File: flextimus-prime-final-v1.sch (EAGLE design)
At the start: 40 parts, among them T1 2N2222, U1 STM32F042K6, U2 IP4220CZ6, U3 MCP1802T-3302I/OT

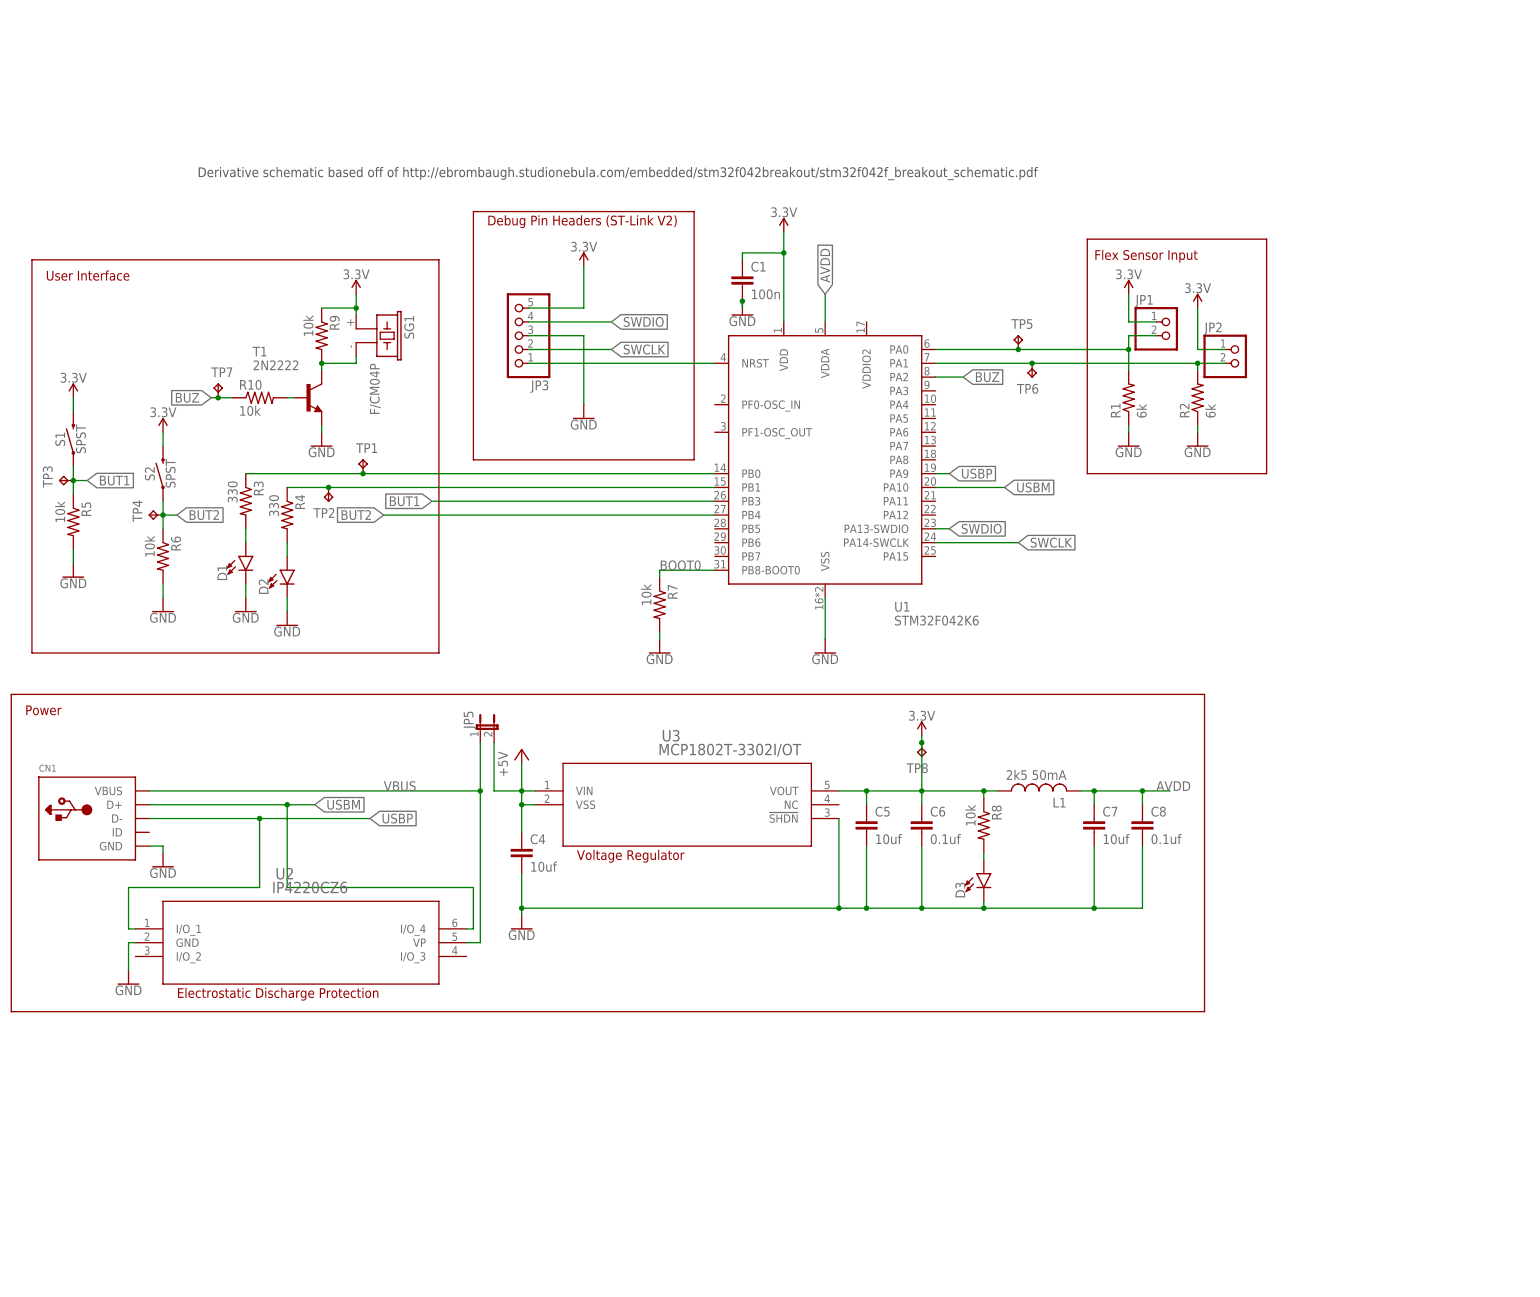
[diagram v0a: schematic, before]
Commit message: Add new board layout and schematic
Also add new lcd driver to use later
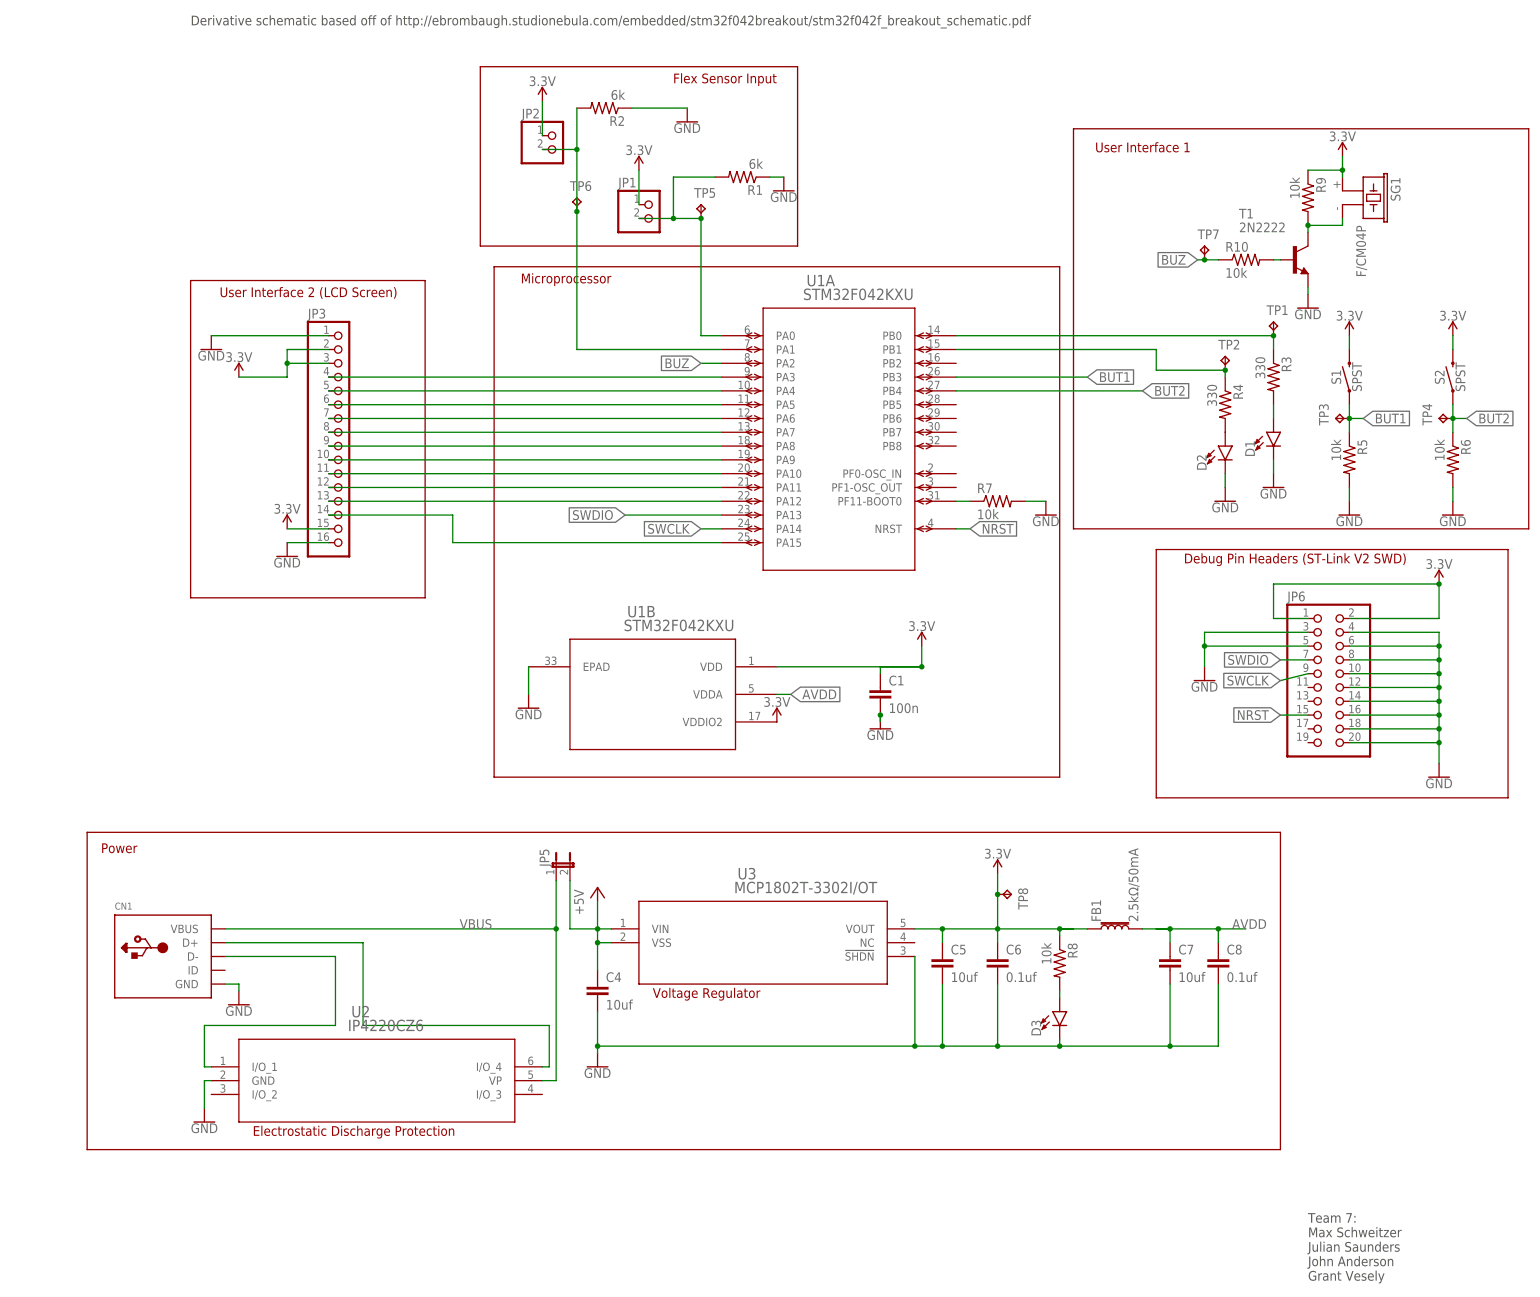
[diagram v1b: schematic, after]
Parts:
- removed L1: 2k5 50mA, rcl:L-USL3216C
- added FB1: 2.5kΩ/50mA, SparkFun-Coils:FERRITE_BEAD-0603
- added JP6: (no value), pinhead:PINHD-2X10
- JP3: device pinhead:PINHD-1X5 -> pinhead:PINHD-1X16
- U1: value STM32F042K6 -> STM32F042KXU; device STM32F042K:STM32F042K6 -> 411test:STM32F042KXU
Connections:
- removed net BOOT0: R7.1, U1.PB8-BOOT0
- new net N$10: JP3.4, U1A.PA3
- new net N$11: JP3.5, U1A.PA4
- new net N$12: JP3.6, U1A.PA5
- new net N$13: JP3.7, U1A.PA6
- new net N$14: JP3.8, U1A.PA7
- new net N$15: JP3.9, U1A.PA8
- new net N$16: JP3.10, U1A.PA9
- new net N$17: JP3.11, U1A.PA10
- new net N$18: JP3.12, U1A.PA11
- new net N$19: JP3.13, U1A.PA12
- new net N$20: R7.1, U1A.PF11-BOOT0
- new net N$21: R4.1, TP2.TP, U1A.PB1
- net 3.3V: now also FB1.1, JP3.15, JP3.2, JP3.3, JP6.1, JP6.2, U1B.VDD, U1B.VDDIO2; no longer JP3.5, L1.1, U1.VDD
- net AVDD: now also FB1.2, U1B.VDDA; no longer L1.2, U1.VDDA
- net BUT1: now also U1A.PB3; no longer U1.PB3
- net BUT2: now also U1A.PB4; no longer U1.PB4
- net BUZ: now also U1A.PA2; no longer U1.PA2
- net GND: now also JP3.1, JP3.16, JP6.10, JP6.12, JP6.14, JP6.16, JP6.18, JP6.20, JP6.3, JP6.4, JP6.5, JP6.6, JP6.8, U1B.EPAD; no longer JP3.3, U1.VSS
- net N$1: now also U1A.PA0; no longer U1.PA0
- net N$2: now also U1A.PA1; no longer U1.PA1
- net N$3: now also U1A.PB0; no longer U1.PB0
- net N$4: now also JP3.14, U1A.PA15; no longer R4.1, TP2.TP, U1.PB1
- net NRST: now also JP6.15, U1A.NRST; no longer JP3.1, U1.NRST
- net SWCLK: now also JP6.9, U1A.PA14; no longer JP3.2, U1.PA14-SWCLK
- net SWDIO: now also JP6.7, U1A.PA13; no longer JP3.4, U1.PA13-SWDIO
- net USBM: no longer U1.PA10
- net USBP: no longer U1.PA9
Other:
- note added: "Debug Pin Headers (ST-Link V2 SWD)"
- note added: "Microprocessor"
- note added: "Team 7: Max Schweitzer Julian Saunders John Anderson Grant Vesely"
- note added: "User Interface 1"
- note added: "User Interface 2 (LCD Screen)"
- note removed: "Debug Pin Headers (ST-Link V2)"
- note removed: "User Interface"
- moved on the sheet: C1, C4, C5, C6, C7, C8, CN1, D1, D2, D3, JP1, JP2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
